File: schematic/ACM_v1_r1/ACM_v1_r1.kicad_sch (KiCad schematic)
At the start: 16 parts, among them J1 DF40C-60DS-0.4V(51), J2 DF40C-60DS-0.4V(51)

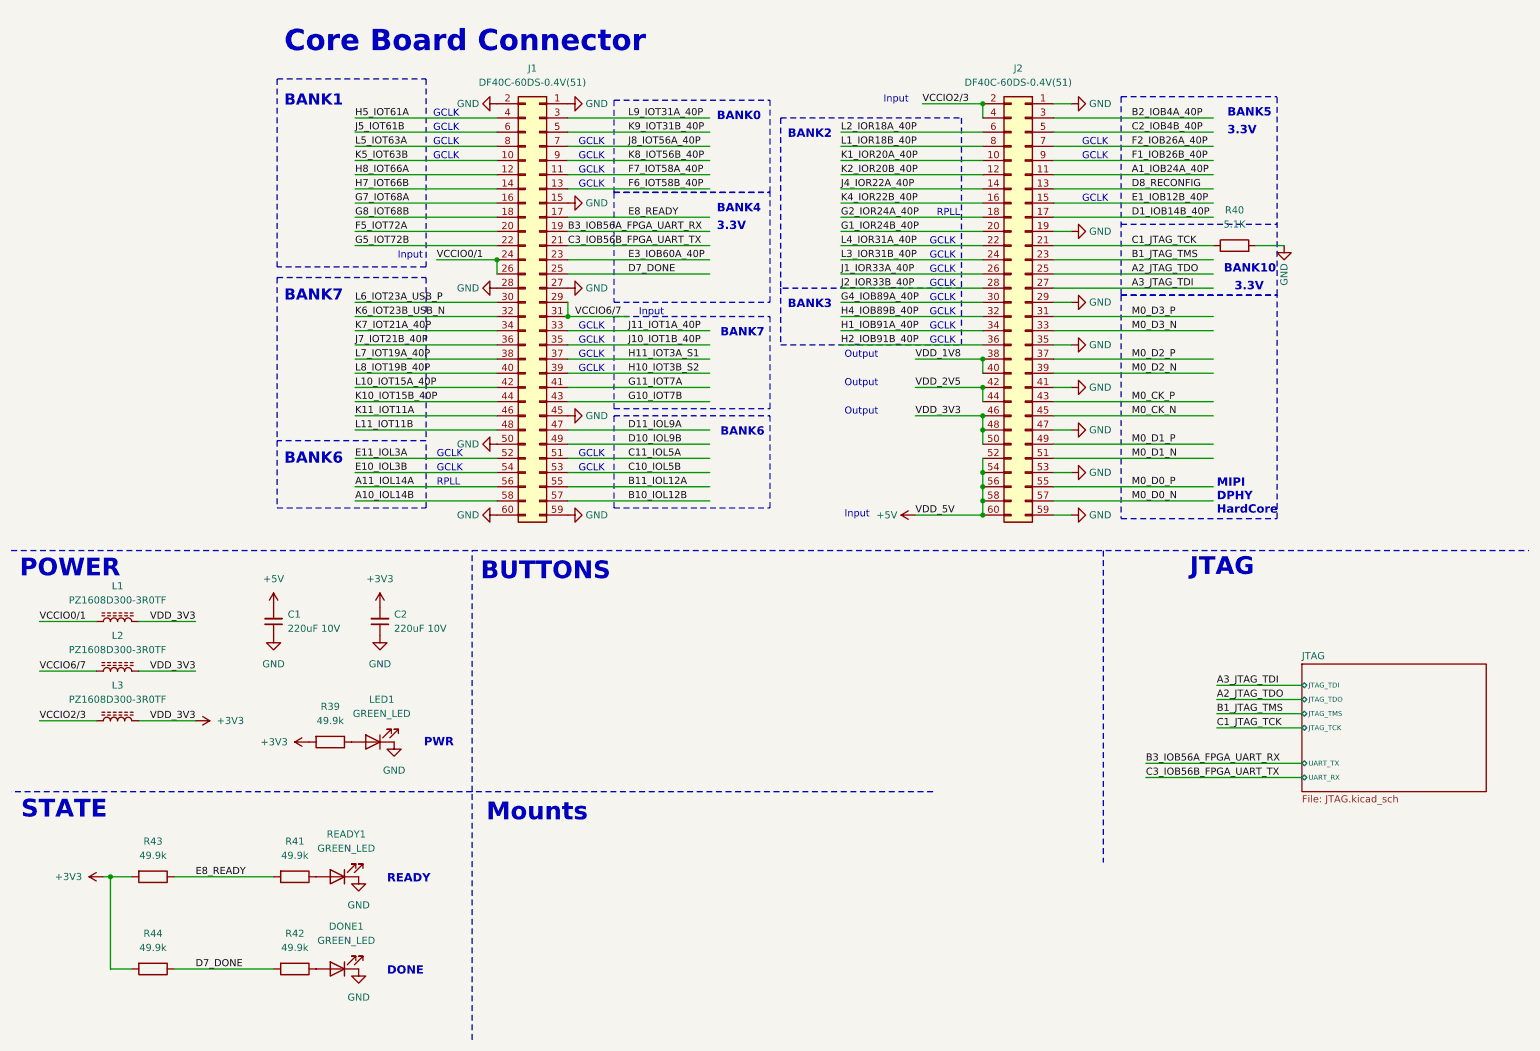
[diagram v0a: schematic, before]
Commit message: ACM module board routed
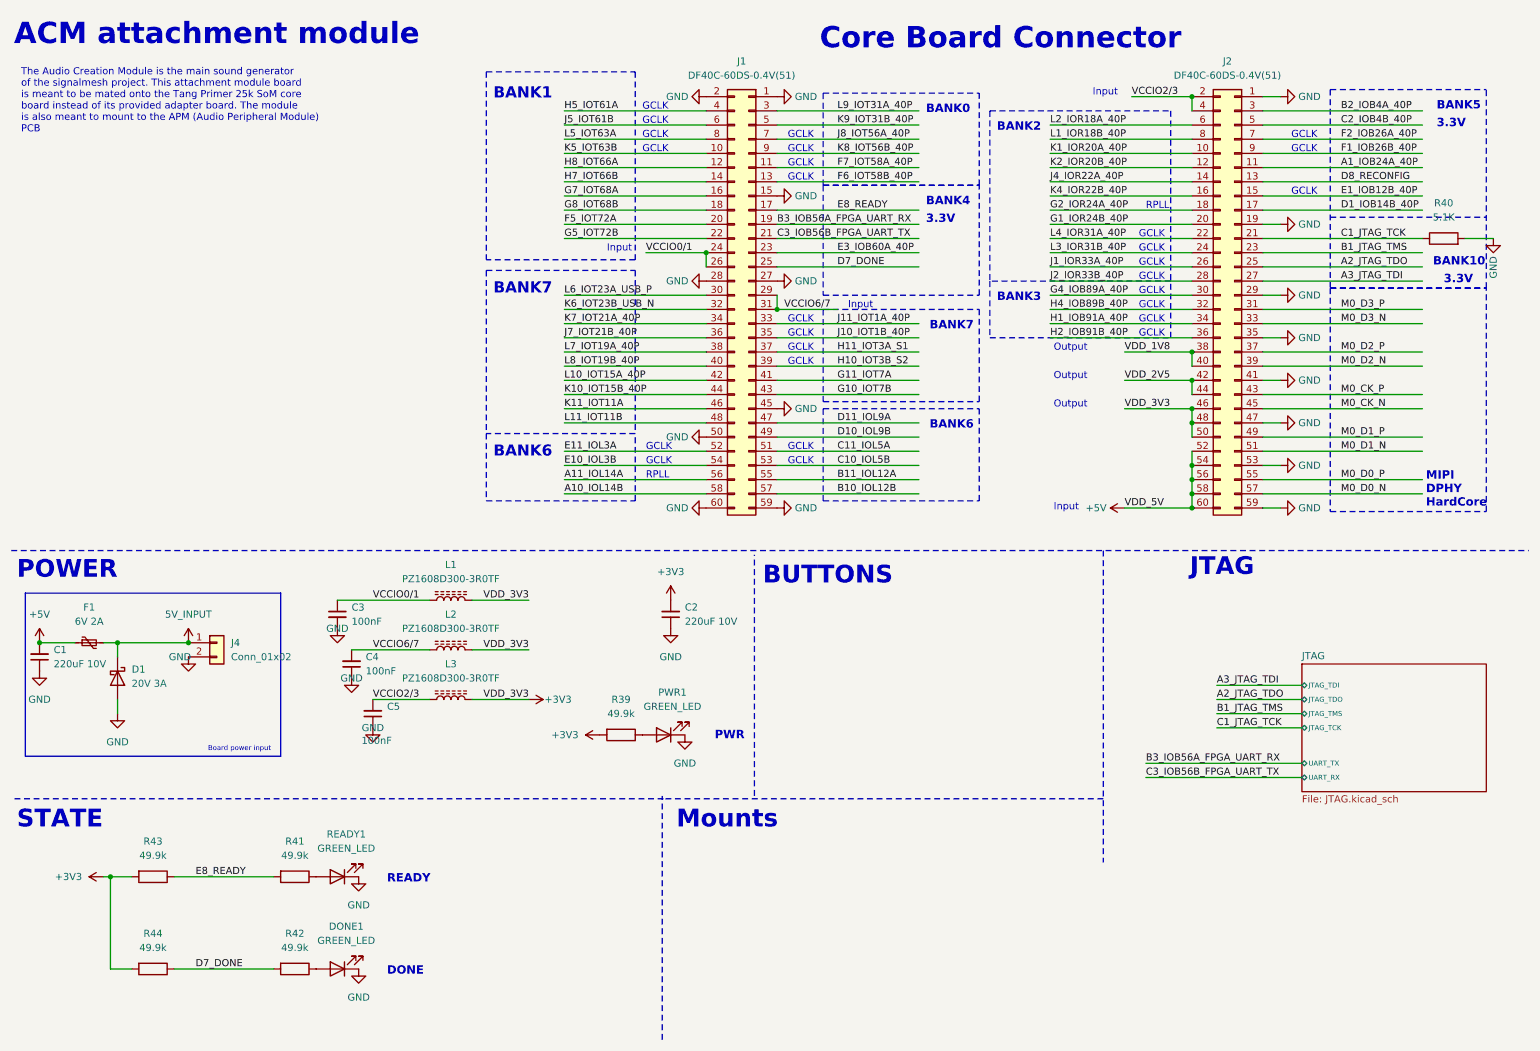
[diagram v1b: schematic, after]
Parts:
- added C3, C4, C5: 100nF, Capacitor_SMD:C_0402_1005Metric, symbol Device:C_Small
- added D1: 20V 3A, Diode_SMD:D_SOD-123, symbol Device:D_Schottky
- added F1: 6V 2A, Fuse:Fuse_0603_1608Metric, symbol Device:Polyfuse_Small
- added J4: Conn_01x02, Connector_PinSocket_2.54mm:PinSocket_1x02_P2.54mm_Vertical_SMD_Pin1Left, symbol Connector_Generic:Conn_01x02
- renumbered LED1 to PWR1
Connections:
- net +5V: now also F1.1
- net GND: now also C3.2, C4.1, C5.1, D1.2 (A), J4.2 (Pin_2)
- net VCCIO0/1: now also C3.1
- net VCCIO2/3: now also C5.2
- net VCCIO6/7: now also C4.2
- new net 5V_INPUT: D1.1 (K), F1.2, J4.1 (Pin_1)
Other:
- note added: "ACM attachment module"
- note added: "Board power input"
- note added: "The Audio Creation Module is the main sound generator of the signalmesh project. This attachment module board is meant to be mated onto the Tang Primer 25k SoM core board instead of its provided adapter board. The module is also meant to mount to the APM (Audio Peripheral Module) PCB"
- moved on the sheet: C1, C2, J1, J2, L1, L2, L3, PWR1, R39, R40

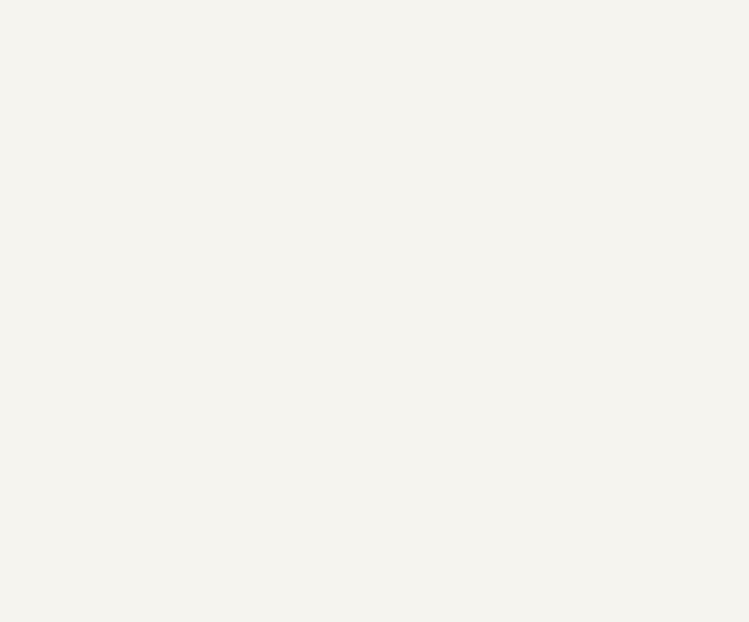
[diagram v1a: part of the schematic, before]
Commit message: add backside connector. fix front connector orientation
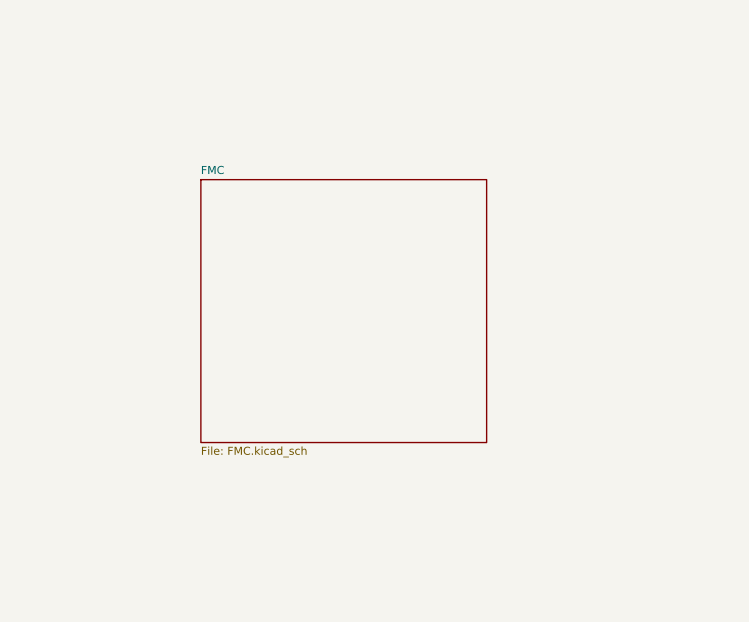
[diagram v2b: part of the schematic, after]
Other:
- added sheet FMC (FMC.kicad_sch)
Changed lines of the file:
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@@
+	)
+	(sheet
+		(at 33.02 54.61)
+		(size 31.75 29.21)
+		(exclude_from_sim no)
+		(in_bom yes)
+		(on_board yes)
+		(dnp no)
+		(fields_autoplaced yes)
+		(stroke
+			(width 0.1524)
+			(type solid)
+		)
+		(fill
+			(color 0 0 0 0)
+		)
+		(property "Sheetname" "FMC"
+			(at 33.02 54.0889 0)
+			(show_name no)
+			(do_not_autoplace no)
+			(effects
+				(font
+					(size 0.889 0.889)
+				)
+				(justify left bottom)
+			)
+		)
+		(property "Sheetfile" "FMC.kicad_sch"
+			(at 33.02 84.2522 0)
+			(show_name no)
+			(do_not_autoplace no)
+			(effects
+				(font
+					(size 0.889 0.889)
+				)
+				(justify left top)
+			)
+		)
+		(instances
+			(project "ACM_v1_r1"
+				(path "/feada479-57f2-4760-a2eb-c5b652c65b2b"
+					(page "3")
+				)
+			)
+		)
 	)
 	(sheet

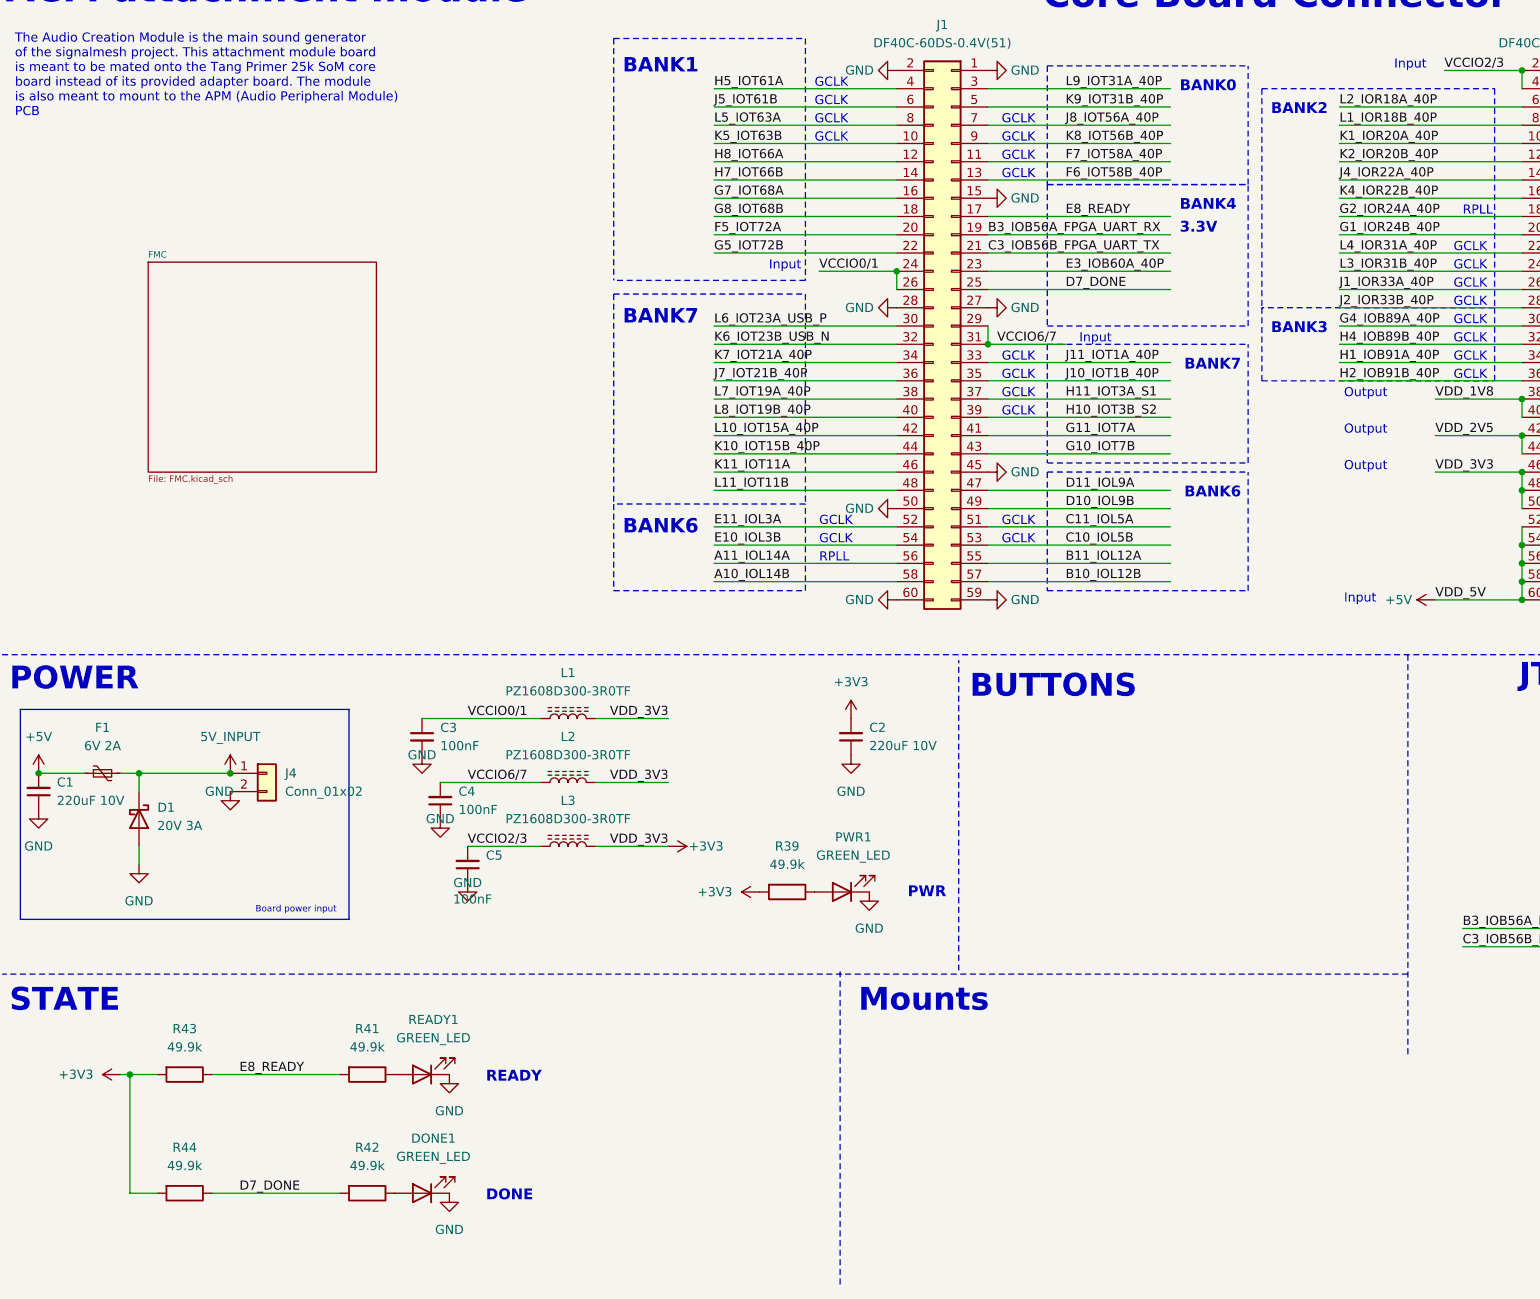
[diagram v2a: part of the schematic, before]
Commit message: figuring out FFC traces next
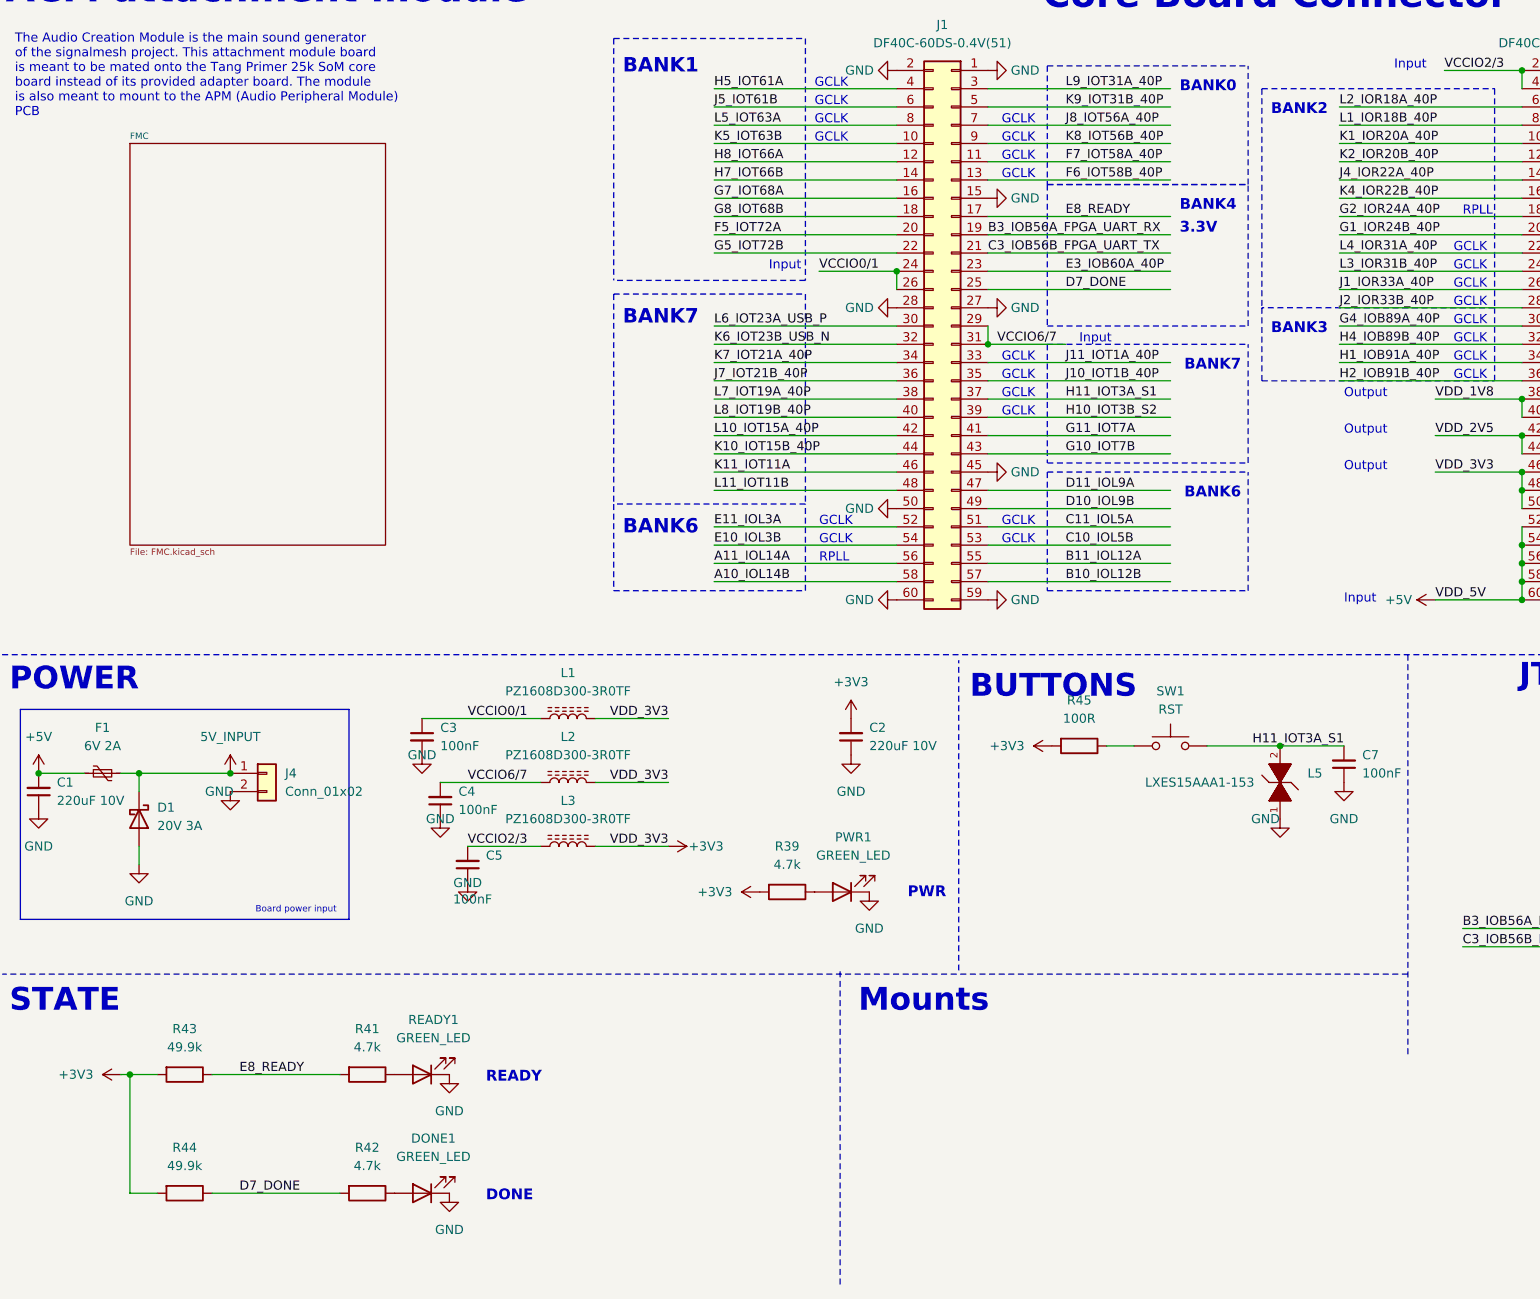
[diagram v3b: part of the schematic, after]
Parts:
- added C7: 100nF, Capacitor_SMD:C_0402_1005Metric, symbol Device:C_Small
- added L5: LXES15AAA1-153, my_footprints:INDC1005X45, symbol LXES15AAA1-153:LXES15AAA1-153
- added R45: 100R, Resistor_SMD:R_0201_0603Metric, symbol Device:R
- added SW1: RST, Button_Switch_SMD:SW_Push_1P1T_NO_CK_KMR2, symbol Switch:SW_Push
- R39, R41, R42: value 49.9k -> 4.7k
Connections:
- net +3V3: now also R45.2
- net GND: now also C7.1, L5.1
- net H11_IOT3A_S1: now also C7.2, L5.2, SW1.2
- new net: R45.1, SW1.1

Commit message: getting ACM and APM schematics put together. tool for FMC pin mapping verif
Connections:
- net +3V3: now also C2.1; no longer C2.2
- net +5V: now also C1.1; no longer C1.2
- net GND: now also C1.2, C2.2; no longer C1.1, C2.1
- no-connect marks 0 -> 11
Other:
- sheet FMC ports: added APM_FPGA_UART_RX, APM_FPGA_UART_TX, FPGA_FMC_A16, FPGA_FMC_A17, FPGA_FMC_A18, FPGA_FMC_A20, FPGA_FMC_A21, FPGA_FMC_A22, FPGA_FMC_A23, FPGA_FMC_A24, FPGA_FMC_CLK, FPGA_FMC_DA0, FPGA_FMC_DA1, FPGA_FMC_DA10, FPGA_FMC_DA11, FPGA_FMC_DA12, FPGA_FMC_DA13, FPGA_FMC_DA14, FPGA_FMC_DA15, FPGA_FMC_DA2, FPGA_FMC_DA3, FPGA_FMC_DA4, FPGA_FMC_DA5, FPGA_FMC_DA6, FPGA_FMC_DA7, FPGA_FMC_DA8, FPGA_FMC_DA9, FPGA_FMC_NE1, FPGA_FMC_NL, FPGA_FMC_NOE, FPGA_FMC_NWAIT, FPGA_FMC_NWE, FPGA_I2C2_SCL, FPGA_I2C2_SDA, FPGA_SPI1_CS, FPGA_SPI1_MISO, FPGA_SPI1_MOSI, FPGA_SPI1_SCK; removed none
- note added: "FPGA Core Board Connector"
- note added: "LEDs"
- note removed: "Core Board Connector"
- note removed: "Mounts"
- note removed: "STATE"
- moved on the sheet: C1, C2, C3, C4, C5, D1, DONE1, F1, J4, L1, L2, L3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
